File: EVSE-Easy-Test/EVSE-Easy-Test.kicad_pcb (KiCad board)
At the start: 2 copper layers, 70.1 x 40.9 mm, 17 parts, among them J1 Type 2, J2 CP diag, SW1 PP current, SW2 CP state

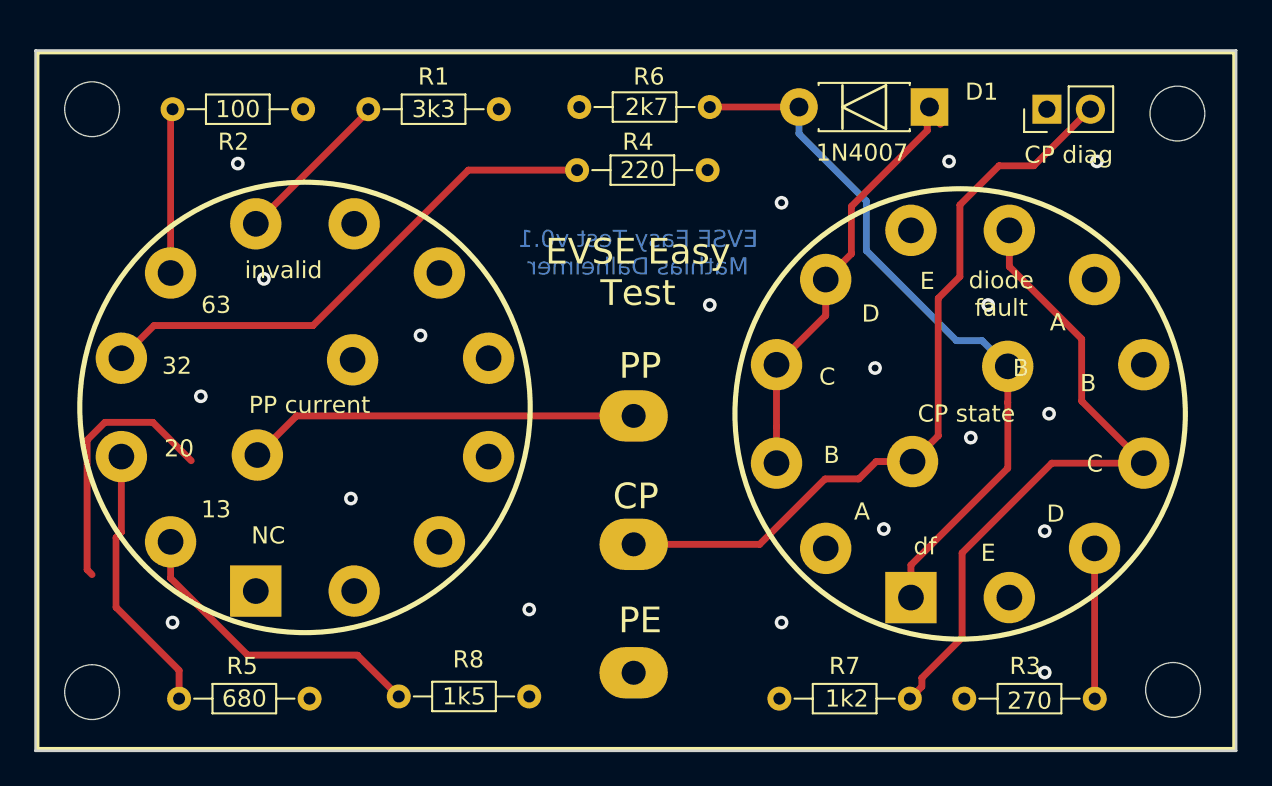
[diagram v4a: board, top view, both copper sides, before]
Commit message: R8 adjusted, some alignments
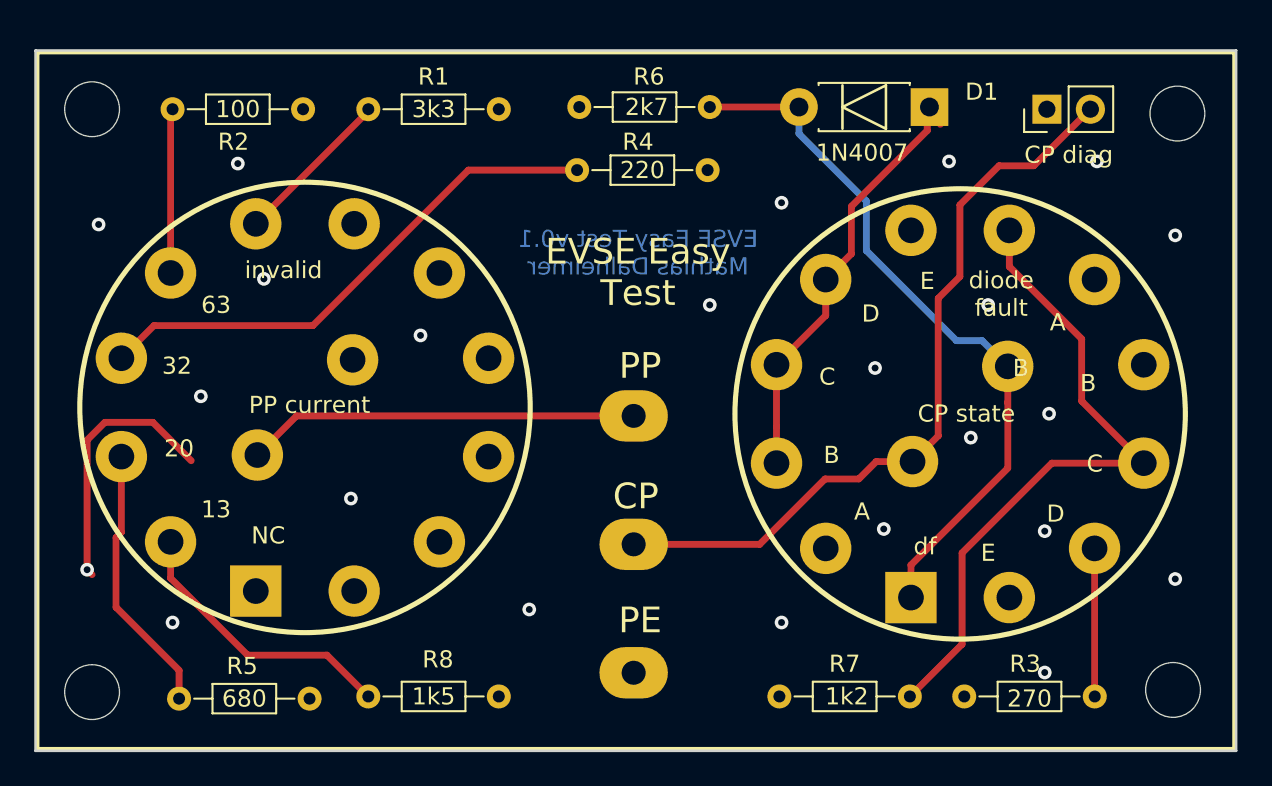
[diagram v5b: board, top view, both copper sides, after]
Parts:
- moved R8 1.78 mm to (67.6, 78.2)
- moved R3 0.13 mm to (94.7, 78.2)
- moved R7 0.13 mm to (83.9, 78.2)
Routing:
- net Net-(R8-Pad2): track 18.3 -> 16.5 mm
- net PE: vias 19 -> 23
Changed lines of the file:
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@@
     (thickness 1.6)
     (drawings 32)
-    (tracks 87)
+    (tracks 90)
     (zones 0)
     (modules 17)
@@
   )
   (module local:R_Axial_DIN0204_L3.6mm_D1.6mm_P7.62mm_Horizontal (layer F.Cu)
-    (at 94.742 78.359)
+    (at 94.742 78.232)
     (descr "Resistor, Axial_DIN0204 series, Axial, Horizontal, pin pitch=7.62mm, 0.16666666666666666W = 1/6W, length*diameter=3.6*1.6mm^2, http://cdn-reichelt.de/documents/datenblatt/B400/1_4W%23YAG.pdf")
     (tags "Resistor Axial_DIN0204 series Axial Horizontal pin pitch 7.62mm 0.16666666666666666W = 1/6W length 3.6mm diameter 1.6mm")
@@
   )
   (module local:R_Axial_DIN0204_L3.6mm_D1.6mm_P7.62mm_Horizontal (layer F.Cu)
-    (at 83.947 78.359)
+    (at 83.947 78.232)
     (descr "Resistor, Axial_DIN0204 series, Axial, Horizontal, pin pitch=7.62mm, 0.16666666666666666W = 1/6W, length*diameter=3.6*1.6mm^2, http://cdn-reichelt.de/documents/datenblatt/B400/1_4W%23YAG.pdf")
     (tags "Resistor Axial_DIN0204 series Axial Horizontal pin pitch 7.62mm 0.16666666666666666W = 1/6W length 3.6mm diameter 1.6mm")
@@
   )
   (module local:R_Axial_DIN0204_L3.6mm_D1.6mm_P7.62mm_Horizontal (layer F.Cu)
-    (at 69.342 78.232 180)
+    (at 67.564 78.232 180)
     (descr "Resistor, Axial_DIN0204 series, Axial, Horizontal, pin pitch=7.62mm, 0.16666666666666666W = 1/6W, length*diameter=3.6*1.6mm^2, http://cdn-reichelt.de/documents/datenblatt/B400/1_4W%23YAG.pdf")
     (tags "Resistor Axial_DIN0204 series Axial Horizontal pin pitch 7.62mm 0.16666666666666666W = 1/6W length 3.6mm diameter 1.6mm")
@@
   (gr_line (start 40.64 40.64) (end 40.64 81.28) (layer F.SilkS) (width 0.2))
   (gr_line (start 40.64 81.28) (end 110.49 81.28) (layer F.SilkS) (width 0.2))
-  (segment (start 93.345 44.825333) (end 93.345 43.815) (width 0.4) (layer F.Cu) (net 2) (status 30))
   (segment (start 97.282 61.07732) (end 97.282 58.956) (width 0.4) (layer F.Cu) (net 1))
   (segment (start 97.282 64.904885) (end 97.282 61.07732) (width 0.4) (layer F.Cu) (net 1))
@@
   (segment (start 95.782001 57.456001) (end 97.282 58.956) (width 0.4) (layer B.Cu) (net 1))
   (segment (start 89.027 52.197) (end 94.286001 57.456001) (width 0.4) (layer B.Cu) (net 1))
+  (segment (start 93.345 44.825333) (end 93.345 43.815) (width 0.4) (layer F.Cu) (net 2) (status 30))
   (segment (start 83.780224 62.487571) (end 83.780224 58.863109) (width 0.4) (layer F.Cu) (net 2))
   (segment (start 83.780224 64.608891) (end 83.780224 62.487571) (width 0.4) (layer F.Cu) (net 2))
@@
   (via (at 52.324 47.117) (size 0.8) (drill 0.4) (layers F.Cu B.Cu) (net 5))
   (via (at 69.342 73.152) (size 0.8) (drill 0.4) (layers F.Cu B.Cu) (net 5))
+  (via (at 44.196 50.673) (size 0.8) (drill 0.4) (layers F.Cu B.Cu) (net 5))
+  (segment (start 43.525223 70.830223) (end 43.525223 70.830223) (width 0.4) (layer F.Cu) (net 5))
+  (via (at 43.525223 70.830223) (size 0.8) (drill 0.4) (layers F.Cu B.Cu) (net 5))
+  (via (at 107.061 51.308) (size 0.8) (drill 0.4) (layers F.Cu B.Cu) (net 5))
+  (via (at 107.061 71.374) (size 0.8) (drill 0.4) (layers F.Cu B.Cu) (net 5))
   (segment (start 59.944 44.063333) (end 59.944 43.942) (width 0.4) (layer F.Cu) (net 6))
   (segment (start 53.374109 50.633224) (end 59.944 44.063333) (width 0.4) (layer F.Cu) (net 6))
@@
   (segment (start 45.525224 68.647776) (end 45.525224 64.227891) (width 0.4) (layer F.Cu) (net 10))
   (segment (start 45.212 68.961) (end 45.525224 68.647776) (width 0.4) (layer F.Cu) (net 10))
-  (segment (start 92.266999 77.659001) (end 92.266999 77.151001) (width 0.4) (layer F.Cu) (net 11))
-  (segment (start 91.567 78.359) (end 92.266999 77.659001) (width 0.4) (layer F.Cu) (net 11))
-  (segment (start 92.266999 77.151001) (end 94.615 74.803) (width 0.4) (layer F.Cu) (net 11))
-  (segment (start 94.615 74.803) (end 94.615 69.85) (width 0.4) (layer F.Cu) (net 11))
-  (segment (start 94.615 69.85) (end 99.856109 64.608891) (width 0.4) (layer F.Cu) (net 11))
-  (segment (start 99.856109 64.608891) (end 105.223776 64.608891) (width 0.4) (layer F.Cu) (net 11))
   (segment (start 97.374891 53.135544) (end 101.6 57.360653) (width 0.4) (layer F.Cu) (net 11))
   (segment (start 97.374891 51.014224) (end 97.374891 53.135544) (width 0.4) (layer F.Cu) (net 11))
   (segment (start 101.6 60.985115) (end 105.223776 64.608891) (width 0.4) (layer F.Cu) (net 11))
   (segment (start 101.6 57.360653) (end 101.6 60.985115) (width 0.4) (layer F.Cu) (net 11))
-  (segment (start 59.309 75.819) (end 61.722 78.232) (width 0.4) (layer F.Cu) (net 12))
+  (segment (start 99.856109 64.608891) (end 105.223776 64.608891) (width 0.4) (layer F.Cu) (net 11))
+  (segment (start 94.615 75.184) (end 94.615 69.85) (width 0.4) (layer F.Cu) (net 11))
+  (segment (start 94.615 69.85) (end 99.856109 64.608891) (width 0.4) (layer F.Cu) (net 11))
+  (segment (start 91.567 78.232) (end 94.615 75.184) (width 0.4) (layer F.Cu) (net 11))
   (segment (start 48.398115 71.325205) (end 52.89191 75.819) (width 0.4) (layer F.Cu) (net 12))
-  (segment (start 52.89191 75.819) (end 59.309 75.819) (width 0.4) (layer F.Cu) (net 12))
   (segment (start 48.398115 69.203885) (end 48.398115 71.325205) (width 0.4) (layer F.Cu) (net 12))
+  (segment (start 59.944 78.232) (end 57.531 75.819) (width 0.4) (layer F.Cu) (net 12))
+  (segment (start 52.89191 75.819) (end 57.531 75.819) (width 0.4) (layer F.Cu) (net 12))
   (zone (net 5) (net_name PE) (layer F.Cu) (hatch edge 0.508)
     (connect_pads (clearance 0.508))
